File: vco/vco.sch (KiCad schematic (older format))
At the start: 61 parts, among them J1 Filtered Power, J13 Octave, J2 SQR, J3 TRI, J4 RMP, J5 1VO, J6 CV, J7 SNC, J8 PWM, J9 FM, U1 TL074, U2 TL072, U3 AS3340, U4 LM4040

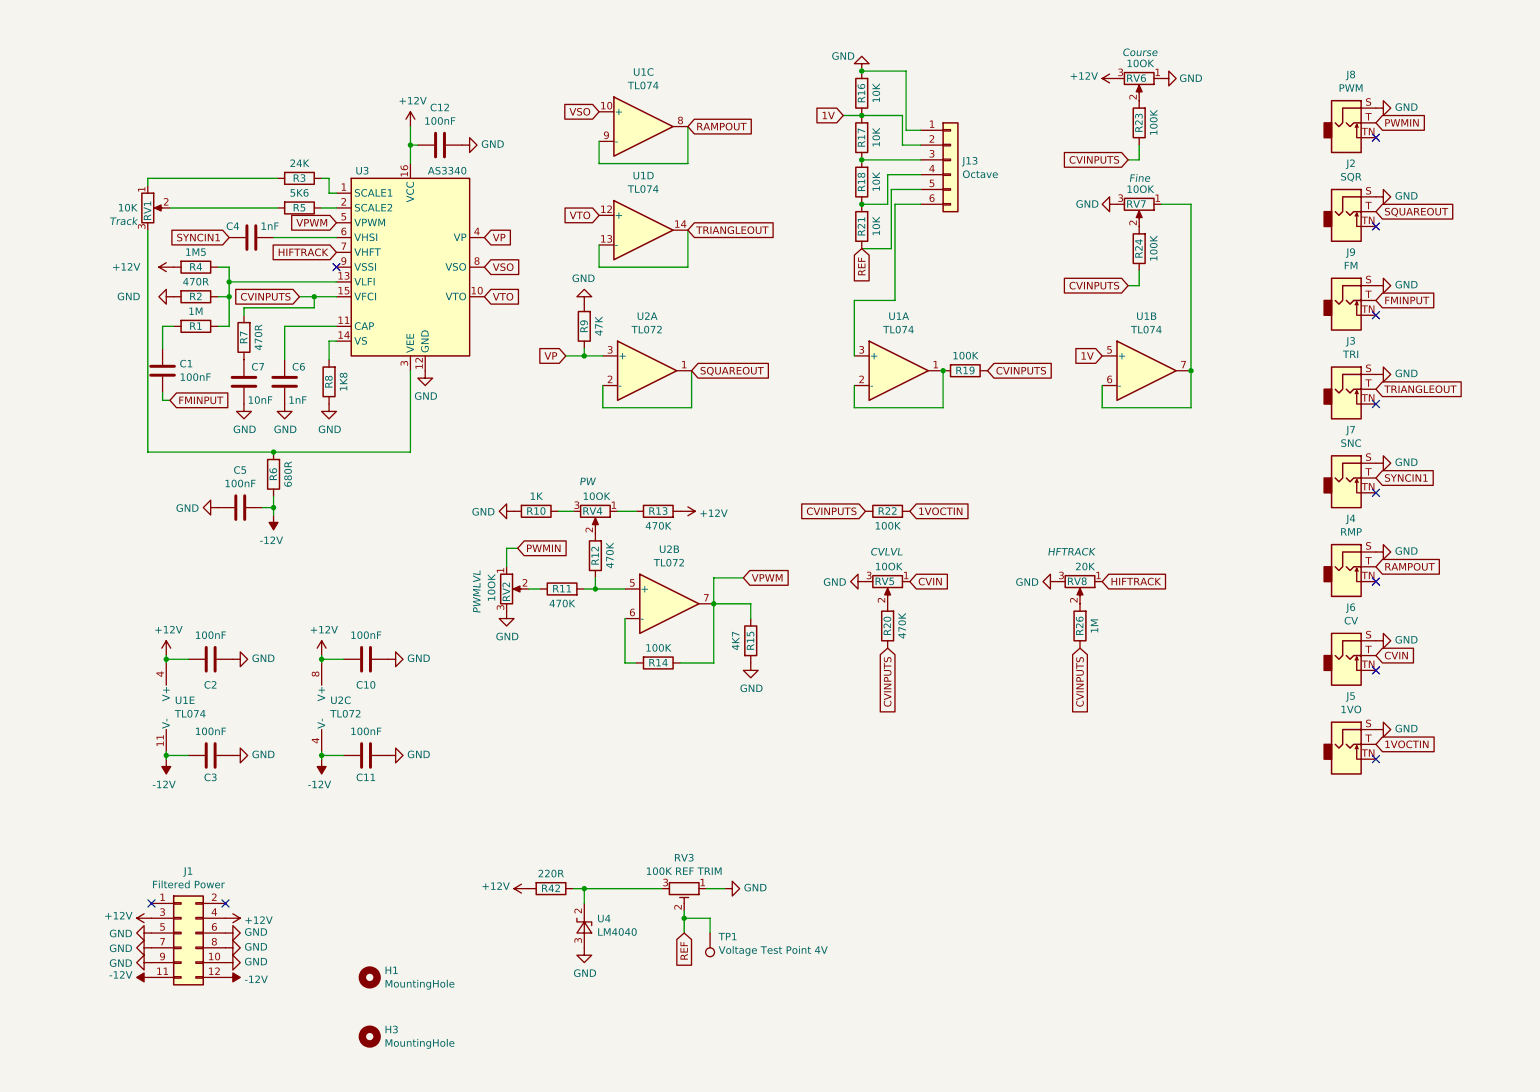
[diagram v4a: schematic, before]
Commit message: All wired up, slightly different layout
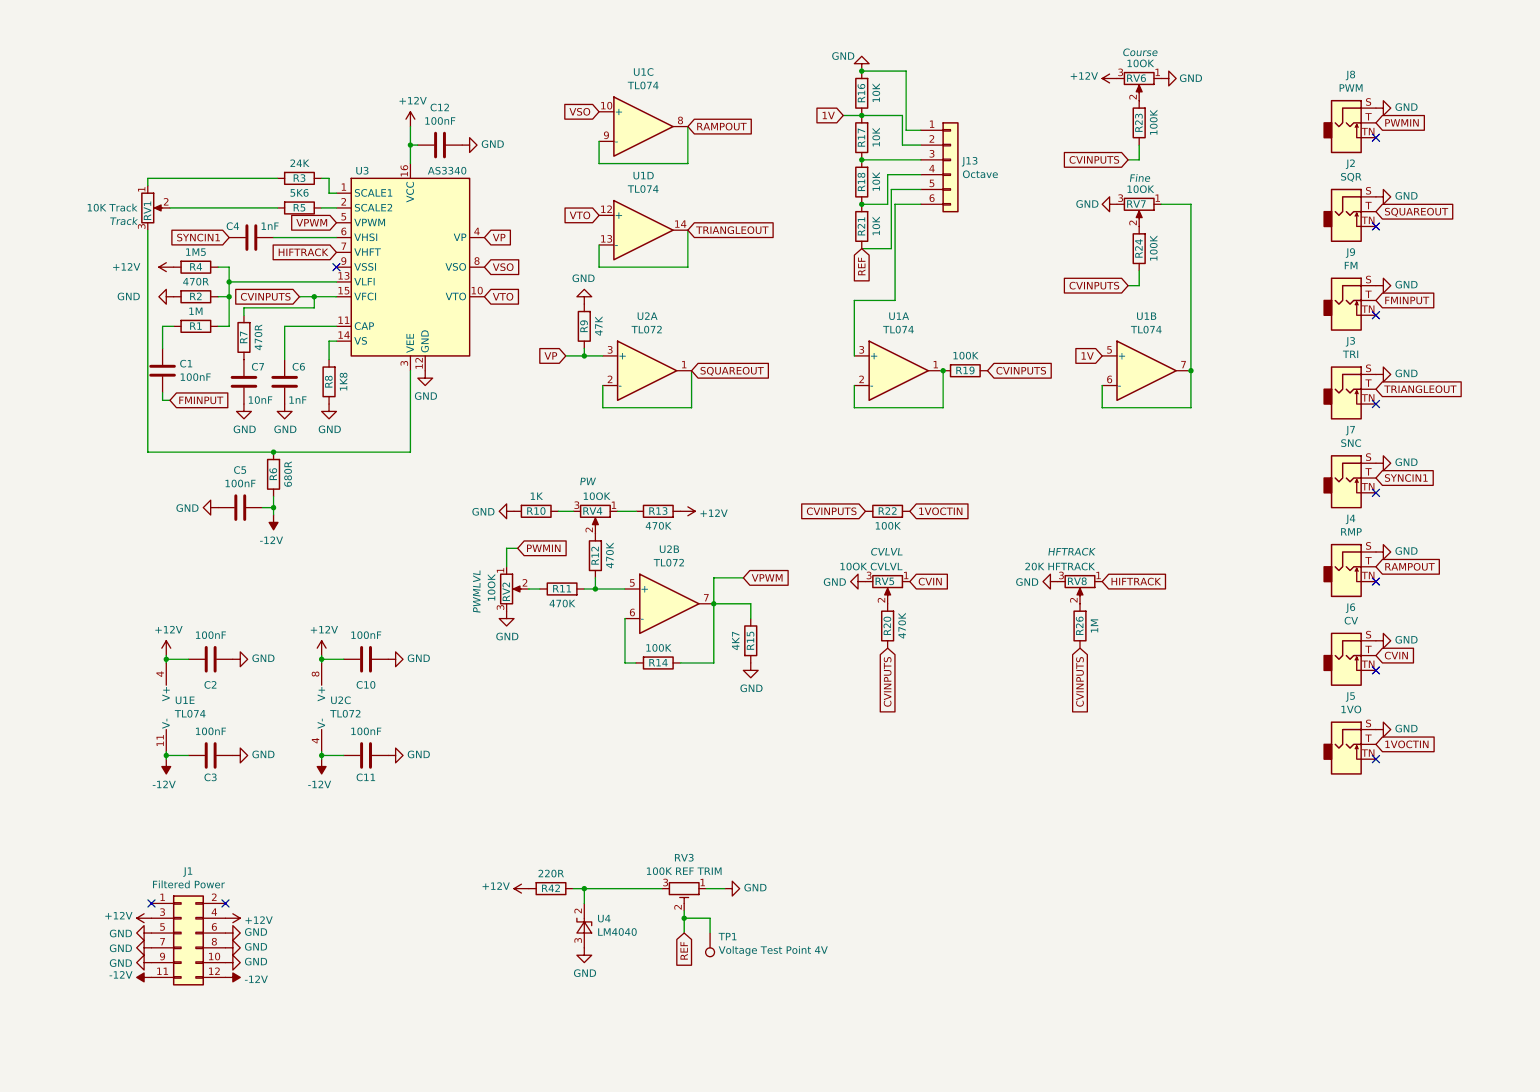
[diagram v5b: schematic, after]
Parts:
- removed H1, H3: MountingHole, MountingHole:MountingHole_3.2mm_M3, symbol Mechanical:MountingHole
- RV1: value 10K -> 10K Track
- RV5: value 10OK -> 10OK CVLVL
- RV8: value 20K -> 20K HFTRACK
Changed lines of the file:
@@
 P 1375 1825
 F 0 "RV1" V 1375 1875 50  0000 R CNN
-F 1 "10K" H 1305 1825 50  0000 R CNN
+F 1 "10K Track" H 1305 1825 50  0000 R CNN
 F 2 "3296W-1-250:TRIM_3296W-1-250" H 1375 1825 50  0001 C CNN
 F 3 "~" H 1375 1825 50  0001 C CNN
@@
 P 6375 4350
 F 0 "RV5" V 6375 4400 50  0000 R CNN
-F 1 "10OK" V 6275 4450 50  0000 R CNN
+F 1 "10OK CVLVL" V 6275 4450 50  0000 R CNN
 F 2 "3296W-1-250:TRIM_3296W-1-250" H 6375 4350 50  0001 C CNN
 F 3 "~" H 6375 4350 50  0001 C CNN
@@
 P 7675 4350
 F 0 "RV8" V 7675 4400 50  0000 R CNN
-F 1 "20K" V 7575 4450 50  0000 R CNN
+F 1 "20K HFTRACK" V 7575 4450 50  0000 R CNN
 F 2 "3296W-1-250:TRIM_3296W-1-250" H 7675 4350 50  0001 C CNN
 F 3 "~" H 7675 4350 50  0001 C CNN
@@
 	0    1    1    0
 $EndComp
-$Comp
-L Mechanical:MountingHole H1
-U 1 1 5E1DA031
-P 2875 7025
-F 0 "H1" H 2975 7071 50  0000 L CNN
-F 1 "MountingHole" H 2975 6980 50  0000 L CNN
-F 2 "MountingHole:MountingHole_3.2mm_M3" H 2875 7025 50  0001 C CNN
-F 3 "~" H 2875 7025 50  0001 C CNN
-	1    2875 7025
-	1    0    0    -1
-$EndComp
-$Comp
-L Mechanical:MountingHole H3
-U 1 1 5E2169CD
-P 2875 7425
-F 0 "H3" H 2975 7471 50  0000 L CNN
-F 1 "MountingHole" H 2975 7380 50  0000 L CNN
-F 2 "MountingHole:MountingHole_3.2mm_M3" H 2875 7425 50  0001 C CNN
-F 3 "~" H 2875 7425 50  0001 C CNN
-	1    2875 7425
-	1    0    0    -1
-$EndComp
 $EndSCHEMATC

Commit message: Started with the panel
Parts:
- added C8, C9: 10uF, Capacitor_THT:CP_Radial_D5.0mm_P2.50mm, symbol Device:CP
- J1: footprint Connector_PinSocket_2.54mm:PinSocket_2x06_P2.54mm_Vertical -> Connector_PinHeader_2.54mm:PinHeader_2x05_P2.54mm_Vertical; symbol Connector_Generic:Conn_02x06_Odd_Even -> Connector_Generic:Conn_02x05_Odd_Even
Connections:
- net +12V: now also J1.1 (Pin_1), J1.2 (Pin_2), C8.1; no longer J1.3 (Pin_3), J1.4 (Pin_4)
- net -12V: now also J1.10 (Pin_10), J1.9 (Pin_9), C9.2; no longer J1.11 (Pin_11), J1.12 (Pin_12)
- net GND: now also J1.3 (Pin_3), J1.4 (Pin_4), C8.2, C9.1; no longer J1.10 (Pin_10), J1.9 (Pin_9)
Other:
- note added: "Basically a copy of LMNCs Performance VCO but meant for the Eurorack format"
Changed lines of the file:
@@
 NoConn ~ 9675 5550
 $Comp
-L Connector_Generic:Conn_02x06_Odd_Even J1
+L Connector_Generic:Conn_02x05_Odd_Even J1
 U 1 1 5E3CD2B4
-P 1600 6725
-F 0 "J1" H 1650 7142 50  0000 C CNN
-F 1 "Filtered Power" H 1650 7051 50  0000 C CNN
-F 2 "Connector_PinSocket_2.54mm:PinSocket_2x06_P2.54mm_Vertical" H 1600 6725 50  0001 C CNN
-F 3 "~" H 1600 6725 50  0001 C CNN
-	1    1600 6725
+P 1600 6825
+F 0 "J1" H 1650 7242 50  0000 C CNN
+F 1 "Filtered Power" H 1650 7151 50  0000 C CNN
+F 2 "Connector_PinHeader_2.54mm:PinHeader_2x05_P2.54mm_Vertical" H 1600 6825 50  0001 C CNN
+F 3 "~" H 1600 6825 50  0001 C CNN
+	1    1600 6825
 	1    0    0    -1
 $EndComp
@@
 	0    1    1    0
 $EndComp
+$Comp
+L Device:CP C8
+U 1 1 5E3F140A
+P 2700 6750
+F 0 "C8" H 2818 6796 50  0000 L CNN
+F 1 "10uF" H 2818 6705 50  0000 L CNN
+F 2 "Capacitor_THT:CP_Radial_D5.0mm_P2.50mm" H 2738 6600 50  0001 C CNN
+F 3 "~" H 2700 6750 50  0001 C CNN
+	1    2700 6750
+	1    0    0    -1
+$EndComp
+$Comp
+L Device:CP C9
+U 1 1 5E3F2AF2
+P 3125 6750
+F 0 "C9" H 3243 6796 50  0000 L CNN
+F 1 "10uF" H 3243 6705 50  0000 L CNN
+F 2 "Capacitor_THT:CP_Radial_D5.0mm_P2.50mm" H 3163 6600 50  0001 C CNN
+F 3 "~" H 3125 6750 50  0001 C CNN
+	1    3125 6750
+	1    0    0    -1
+$EndComp
+$Comp
+L power:+12V #PWR01
+U 1 1 5E3F34A0
+P 2700 6600
+F 0 "#PWR01" H 2700 6450 50  0001 C CNN
+F 1 "+12V" V 2715 6728 50  0000 L CNN
+F 2 "" H 2700 6600 50  0001 C CNN
+F 3 "" H 2700 6600 50  0001 C CNN
+	1    2700 6600
+	1    0    0    -1
+$EndComp
+$Comp
+L power:-12V #PWR04
+U 1 1 5E3F4152
+P 3125 6900
+F 0 "#PWR04" H 3125 7000 50  0001 C CNN
+F 1 "-12V" V 3140 7028 50  0000 L CNN
+F 2 "" H 3125 6900 50  0001 C CNN
+F 3 "" H 3125 6900 50  0001 C CNN
+	1    3125 6900
+	-1   0    0    1
+$EndComp
+$Comp
+L power:GND #PWR02
+U 1 1 5E3F4D70
+P 2700 6900
+F 0 "#PWR02" H 2700 6650 50  0001 C CNN
+F 1 "GND" V 2705 6772 50  0000 R CNN
+F 2 "" H 2700 6900 50  0001 C CNN
+F 3 "" H 2700 6900 50  0001 C CNN
+	1    2700 6900
+	1    0    0    -1
+$EndComp
+$Comp
+L power:GND #PWR03
+U 1 1 5E3F59B8
+P 3125 6600
+F 0 "#PWR03" H 3125 6350 50  0001 C CNN
+F 1 "GND" V 3130 6472 50  0000 R CNN
+F 2 "" H 3125 6600 50  0001 C CNN
+F 3 "" H 3125 6600 50  0001 C CNN
+	1    3125 6600
+	-1   0    0    1
+$EndComp
+Text Notes 7050 6675 0    50   ~ 0
+Basically a copy of LMNCs Performance VCO but meant for the Eurorack format
 $EndSCHEMATC
